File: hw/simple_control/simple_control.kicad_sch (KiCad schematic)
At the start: 4 parts, among them J101 Screw_Terminal_01x02, J102 Jack-DC, J103 Screw_Terminal_01x03, J104 Screw_Terminal_01x03

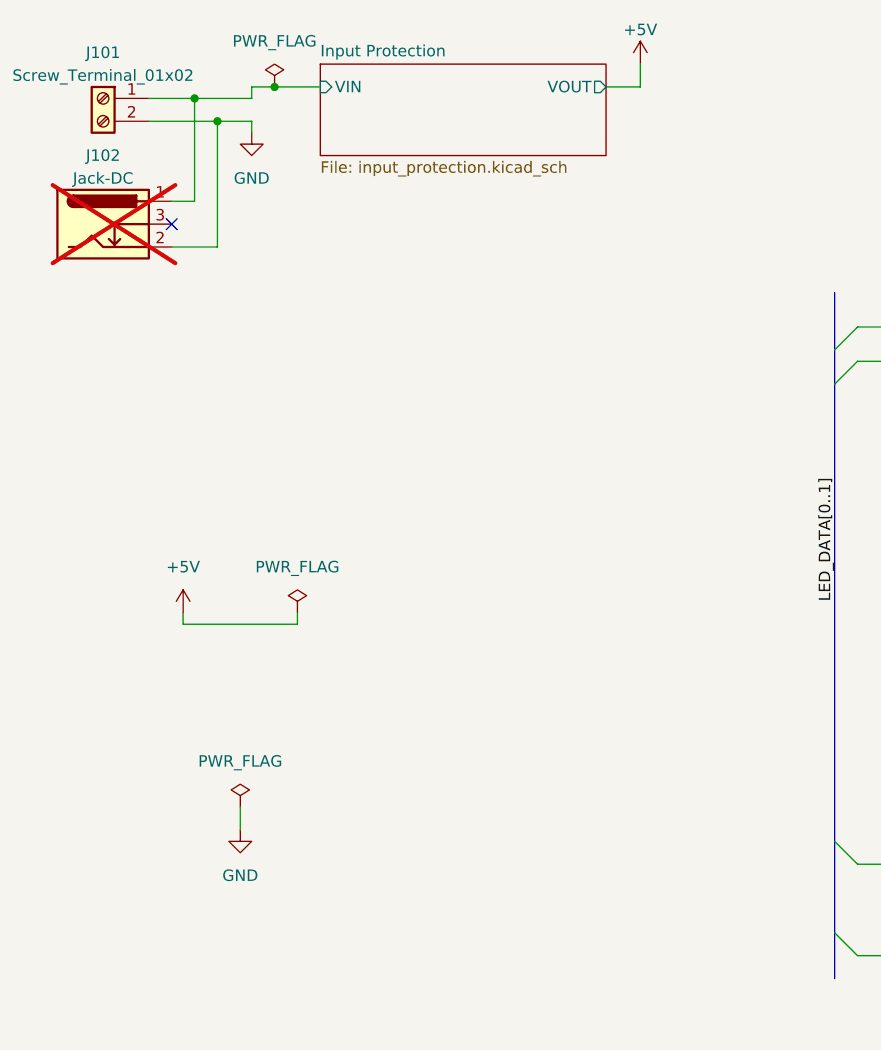
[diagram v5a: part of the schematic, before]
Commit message: chore(hw): wire LEDs to Pico, other improvements
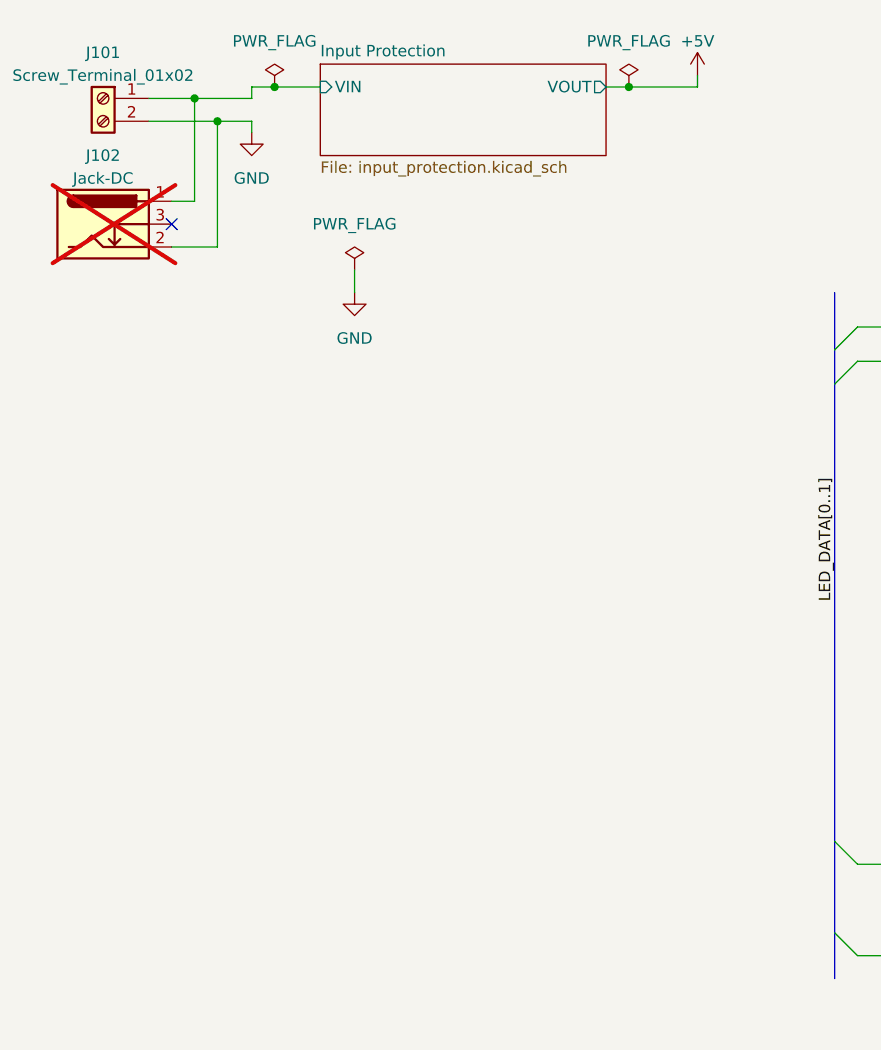
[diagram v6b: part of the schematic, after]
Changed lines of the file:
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@@
     (comment 1 "Main Connectors")
+  )
+  (junction (at 90.17 45.72) (diameter 0) (color 0 0 0 0)
   )
   (junction (at 44.45 49.53) (diameter 0) (color 0 0 0 0)
@@
     (stroke (width 0) (type default))
   )
+  (wire (pts (xy 90.17 45.72) (xy 97.79 45.72))
+    (stroke (width 0) (type default))
+  )
   (wire (pts (xy 50.8 45.72) (xy 55.88 45.72))
     (stroke (width 0) (type default))
   )
-  (wire (pts (xy 91.44 45.72) (xy 91.44 43.18))
+  (wire (pts (xy 97.79 45.72) (xy 97.79 44.45))
     (stroke (width 0) (type default))
   )
@@
     (stroke (width 0) (type default))
   )
-  (wire (pts (xy 40.64 104.14) (xy 40.64 105.41))
-    (stroke (width 0) (type default))
-  )
   (wire (pts (xy 184.15 147.32) (xy 191.77 147.32))
     (stroke (width 0) (type default))
@@
     (stroke (width 0) (type default))
   )
-  (wire (pts (xy 87.63 45.72) (xy 91.44 45.72))
+  (wire (pts (xy 87.63 45.72) (xy 90.17 45.72))
     (stroke (width 0) (type default))
   )
@@
     (stroke (width 0) (type default))
   )
-  (wire (pts (xy 40.64 105.41) (xy 53.34 105.41))
-    (stroke (width 0) (type default))
-  )
   (bus (pts (xy 120.65 55.88) (xy 120.65 66.04))
     (stroke (width 0) (type default))
@@
     (stroke (width 0) (type default))
   )
-  (wire (pts (xy 46.99 125.73) (xy 46.99 128.27))
+  (wire (pts (xy 59.69 66.04) (xy 59.69 68.58))
     (stroke (width 0) (type default))
   )
@@
   )
   (wire (pts (xy 115.57 72.39) (xy 162.56 72.39))
-    (stroke (width 0) (type default))
-  )
-  (wire (pts (xy 53.34 105.41) (xy 53.34 104.14))
     (stroke (width 0) (type default))
   )
@@
     )
   )
-  (symbol (lib_id "power:+5V") (at 40.64 104.14 0) (unit 1)
-    (in_bom yes) (on_board yes) (dnp no) (fields_autoplaced)
-    (property "Reference" "#PWR0103" (at 40.64 107.95 0)
-      (effects (font (size 1.27 1.27)) hide)
-    )
-    (property "Value" "+5V" (at 40.64 99.06 0)
-      (effects (font (size 1.27 1.27)))
-    )
-    (property "Footprint" "" (at 40.64 104.14 0)
-      (effects (font (size 1.27 1.27)) hide)
-    )
-    (property "Datasheet" "" (at 40.64 104.14 0)
-      (effects (font (size 1.27 1.27)) hide)
-    )
-    (pin "1")
-    (instances
-      (project "simple_control"
-        (path "/063164e8-0d2a-492b-8a61-e4fa4fbf06a6"
-          (reference "#PWR0103") (unit 1)
-        )
-      )
-    )
-  )
-  (symbol (lib_id "power:PWR_FLAG") (at 46.99 125.73 0) (unit 1)
-    (in_bom yes) (on_board yes) (dnp no) (fields_autoplaced)
-    (property "Reference" "#FLG0103" (at 46.99 123.825 0)
-      (effects (font (size 1.27 1.27)) hide)
-    )
-    (property "Value" "PWR_FLAG" (at 46.99 120.65 0)
-      (effects (font (size 1.27 1.27)))
-    )
-    (property "Footprint" "" (at 46.99 125.73 0)
-      (effects (font (size 1.27 1.27)) hide)
-    )
-    (property "Datasheet" "~" (at 46.99 125.73 0)
+  (symbol (lib_id "power:PWR_FLAG") (at 59.69 66.04 0) (unit 1)
+    (in_bom yes) (on_board yes) (dnp no) (fields_autoplaced)
+    (property "Reference" "#FLG0103" (at 59.69 64.135 0)
+      (effects (font (size 1.27 1.27)) hide)
+    )
+    (property "Value" "PWR_FLAG" (at 59.69 60.96 0)
+      (effects (font (size 1.27 1.27)))
+    )
+    (property "Footprint" "" (at 59.69 66.04 0)
+      (effects (font (size 1.27 1.27)) hide)
+    )
+    (property "Datasheet" "~" (at 59.69 66.04 0)
       (effects (font (size 1.27 1.27)) hide)
     )
@@
     )
   )
-  (symbol (lib_id "power:+5V") (at 91.44 43.18 0) (unit 1)
-    (in_bom yes) (on_board yes) (dnp no) (fields_autoplaced)
-    (property "Reference" "#PWR0101" (at 91.44 46.99 0)
-      (effects (font (size 1.27 1.27)) hide)
-    )
-    (property "Value" "+5V" (at 91.44 39.37 0)
-      (effects (font (size 1.27 1.27)))
-    )
-    (property "Footprint" "" (at 91.44 43.18 0)
-      (effects (font (size 1.27 1.27)) hide)
-    )
-    (property "Datasheet" "" (at 91.44 43.18 0)
+  (symbol (lib_id "power:+5V") (at 97.79 44.45 0) (unit 1)
+    (in_bom yes) (on_board yes) (dnp no) (fields_autoplaced)
+    (property "Reference" "#PWR0101" (at 97.79 48.26 0)
+      (effects (font (size 1.27 1.27)) hide)
+    )
+    (property "Value" "+5V" (at 97.79 40.64 0)
+      (effects (font (size 1.27 1.27)))
+    )
+    (property "Footprint" "" (at 97.79 44.45 0)
+      (effects (font (size 1.27 1.27)) hide)
+    )
+    (property "Datasheet" "" (at 97.79 44.45 0)
       (effects (font (size 1.27 1.27)) hide)
     )
@@
     )
   )
-  (symbol (lib_id "power:GND") (at 46.99 128.27 0) (unit 1)
-    (in_bom yes) (on_board yes) (dnp no) (fields_autoplaced)
-    (property "Reference" "#PWR0106" (at 46.99 134.62 0)
-      (effects (font (size 1.27 1.27)) hide)
-    )
-    (property "Value" "GND" (at 46.99 133.35 0)
-      (effects (font (size 1.27 1.27)))
-    )
-    (property "Footprint" "" (at 46.99 128.27 0)
-      (effects (font (size 1.27 1.27)) hide)
-    )
-    (property "Datasheet" "" (at 46.99 128.27 0)
+  (symbol (lib_id "power:GND") (at 59.69 68.58 0) (unit 1)
+    (in_bom yes) (on_board yes) (dnp no) (fields_autoplaced)
+    (property "Reference" "#PWR0106" (at 59.69 74.93 0)
+      (effects (font (size 1.27 1.27)) hide)
+    )
+    (property "Value" "GND" (at 59.69 73.66 0)
+      (effects (font (size 1.27 1.27)))
+    )
+    (property "Footprint" "" (at 59.69 68.58 0)
+      (effects (font (size 1.27 1.27)) hide)
+    )
+    (property "Datasheet" "" (at 59.69 68.58 0)
       (effects (font (size 1.27 1.27)) hide)
     )
@@
     )
   )
-  (symbol (lib_id "power:PWR_FLAG") (at 53.34 104.14 0) (unit 1)
-    (in_bom yes) (on_board yes) (dnp no) (fields_autoplaced)
-    (property "Reference" "#FLG0102" (at 53.34 102.235 0)
-      (effects (font (size 1.27 1.27)) hide)
-    )
-    (property "Value" "PWR_FLAG" (at 53.34 99.06 0)
-      (effects (font (size 1.27 1.27)))
-    )
-    (property "Footprint" "" (at 53.34 104.14 0)
-      (effects (font (size 1.27 1.27)) hide)
-    )
-    (property "Datasheet" "~" (at 53.34 104.14 0)
-      (effects (font (size 1.27 1.27)) hide)
-    )
+  (symbol (lib_id "power:PWR_FLAG") (at 90.17 45.72 0) (unit 1)
+    (in_bom yes) (on_board yes) (dnp no) (fields_autoplaced)
+    (property "Reference" "#FLG0102" (at 90.17 43.815 0)
+      (effects (font (size 1.27 1.27)) hide)
+    )
+    (property "Value" "PWR_FLAG" (at 90.17 40.64 0)
+      (effects (font (size 1.27 1.27)))
+    )
+    (property "Footprint" "" (at 90.17 45.72 0)
+      (effects (font (size 1.27 1.27)) hide)
+    )
+    (property "Datasheet" "~" (at 90.17 45.72 0)
+      (effects (font (size 1.27 1.27)) hide)
+    )

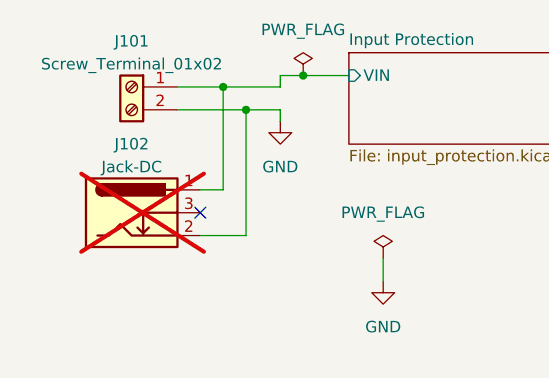
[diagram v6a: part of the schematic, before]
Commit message: chore(hw): layout the power input circuit
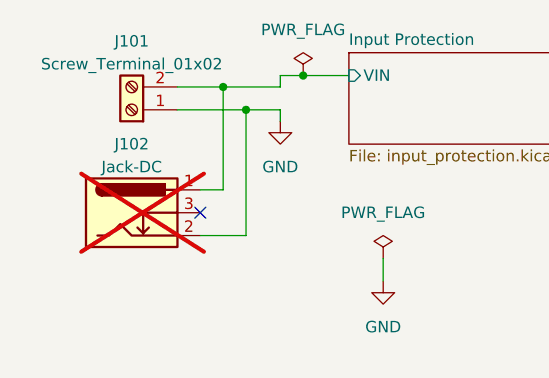
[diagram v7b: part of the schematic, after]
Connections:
- net GND: now also J101.1 (Pin_1); no longer J101.2 (Pin_2)
- net Input Protection/VIN: now also J101.2 (Pin_2); no longer J101.1 (Pin_1)
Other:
- moved on the sheet: J101
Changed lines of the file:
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@@
     )
   )
-  (symbol (lib_id "Connector:Screw_Terminal_01x02") (at 31.75 46.99 0) (mirror y) (unit 1)
-    (in_bom yes) (on_board yes) (dnp no) (fields_autoplaced)
+  (symbol (lib_id "Connector:Screw_Terminal_01x02") (at 31.75 49.53 180) (unit 1)
+    (in_bom yes) (on_board yes) (dnp no)
     (property "Reference" "J101" (at 31.75 41.91 0)
       (effects (font (size 1.27 1.27)))
@@
       (effects (font (size 1.27 1.27)))
     )
-    (property "Footprint" "TerminalBlock_Phoenix:TerminalBlock_Phoenix_MKDS-1,5-2_1x02_P5.00mm_Horizontal" (at 31.75 46.99 0)
+    (property "Footprint" "TerminalBlock_Phoenix:TerminalBlock_Phoenix_MKDS-1,5-2_1x02_P5.00mm_Horizontal" (at 31.75 49.53 0)
       (effects (font (size 1.27 1.27)) hide)
     )
-    (property "Datasheet" "~" (at 31.75 46.99 0)
+    (property "Datasheet" "~" (at 31.75 49.53 0)
       (effects (font (size 1.27 1.27)) hide)
     )

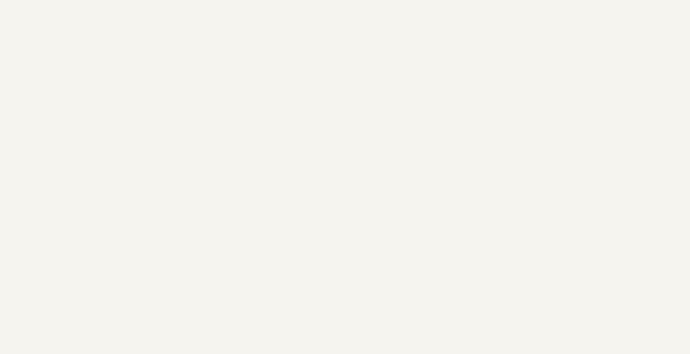
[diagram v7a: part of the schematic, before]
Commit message: chore(hw): add mounting holes and connect power planes
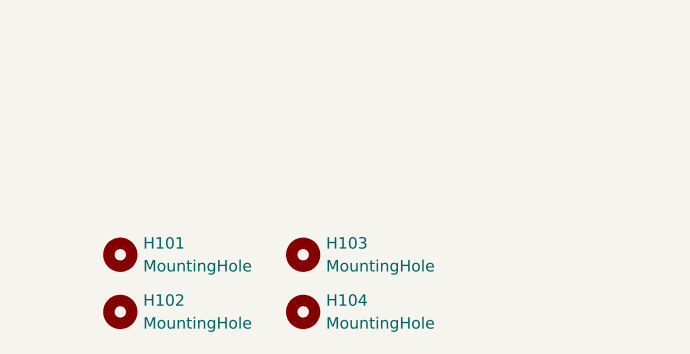
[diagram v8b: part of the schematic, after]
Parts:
- added H101, H102, H103, H104: MountingHole, MountingHole:MountingHole_2.7mm_M2.5, symbol Mechanical:MountingHole
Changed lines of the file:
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@@
+    )
+  )
+  (symbol (lib_id "Mechanical:MountingHole") (at 50.8 162.56 0) (unit 1)
+    (in_bom yes) (on_board yes) (dnp no) (fields_autoplaced)
+    (property "Reference" "H103" (at 53.34 161.29 0)
+      (effects (font (size 1.27 1.27)) (justify left))
+    )
+    (property "Value" "MountingHole" (at 53.34 163.83 0)
+      (effects (font (size 1.27 1.27)) (justify left))
+    )
+    (property "Footprint" "MountingHole:MountingHole_2.7mm_M2.5" (at 50.8 162.56 0)
+      (effects (font (size 1.27 1.27)) hide)
+    )
+    (property "Datasheet" "~" (at 50.8 162.56 0)
+      (effects (font (size 1.27 1.27)) hide)
+    )
+    (instances
+      (project "simple_control"
+        (path "/063164e8-0d2a-492b-8a61-e4fa4fbf06a6"
+          (reference "H103") (unit 1)
+        )
+      )
     )
   )
@@
     )
   )
+  (symbol (lib_id "Mechanical:MountingHole") (at 30.48 168.91 0) (unit 1)
+    (in_bom yes) (on_board yes) (dnp no) (fields_autoplaced)
+    (property "Reference" "H102" (at 33.02 167.64 0)
+      (effects (font (size 1.27 1.27)) (justify left))
+    )
+    (property "Value" "MountingHole" (at 33.02 170.18 0)
+      (effects (font (size 1.27 1.27)) (justify left))
+    )
+    (property "Footprint" "MountingHole:MountingHole_2.7mm_M2.5" (at 30.48 168.91 0)
+      (effects (font (size 1.27 1.27)) hide)
+    )
+    (property "Datasheet" "~" (at 30.48 168.91 0)
+      (effects (font (size 1.27 1.27)) hide)
+    )
+    (instances
+      (project "simple_control"
+        (path "/063164e8-0d2a-492b-8a61-e4fa4fbf06a6"
+          (reference "H102") (unit 1)
+        )
+      )
+    )
+  )
   (symbol (lib_id "Connector:Barrel_Jack_Switch") (at 31.75 60.96 0) (unit 1)
     (in_bom yes) (on_board yes) (dnp yes) (fields_autoplaced)
@@
     )
   )
+  (symbol (lib_id "Mechanical:MountingHole") (at 50.8 168.91 0) (unit 1)
+    (in_bom yes) (on_board yes) (dnp no) (fields_autoplaced)
+    (property "Reference" "H104" (at 53.34 167.64 0)
+      (effects (font (size 1.27 1.27)) (justify left))
+    )
+    (property "Value" "MountingHole" (at 53.34 170.18 0)
+      (effects (font (size 1.27 1.27)) (justify left))
+    )
+    (property "Footprint" "MountingHole:MountingHole_2.7mm_M2.5" (at 50.8 168.91 0)
+      (effects (font (size 1.27 1.27)) hide)
+    )
+    (property "Datasheet" "~" (at 50.8 168.91 0)
+      (effects (font (size 1.27 1.27)) hide)
+    )
+    (instances
+      (project "simple_control"
+        (path "/063164e8-0d2a-492b-8a61-e4fa4fbf06a6"
+          (reference "H104") (unit 1)
+        )
+      )
+    )
+  )
   (symbol (lib_id "power:GND") (at 191.77 151.13 0) (unit 1)
     (in_bom yes) (on_board yes) (dnp no)
@@
         )
       )
+    )
+  )
+  (symbol (lib_id "Mechanical:MountingHole") (at 30.48 162.56 0) (unit 1)
+    (in_bom yes) (on_board yes) (dnp no) (fields_autoplaced)
+    (property "Reference" "H101" (at 33.02 161.29 0)
+      (effects (font (size 1.27 1.27)) (justify left))
+    )
+    (property "Value" "MountingHole" (at 33.02 163.83 0)
+      (effects (font (size 1.27 1.27)) (justify left))
+    )
+    (property "Footprint" "MountingHole:MountingHole_2.7mm_M2.5" (at 30.48 162.56 0)
+      (effects (font (size 1.27 1.27)) hide)
+    )
+    (property "Datasheet" "~" (at 30.48 162.56 0)
+      (effects (font (size 1.27 1.27)) hide)
+    )
+    (instances
+      (project "simple_control"
+        (path "/063164e8-0d2a-492b-8a61-e4fa4fbf06a6"
+          (reference "H101") (unit 1)
+        )
+      )
